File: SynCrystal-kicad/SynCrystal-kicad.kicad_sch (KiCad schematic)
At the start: 75 parts, among them J1 ICSP, J2 Projector, Q1 BC847, Q2 BC847, SW1 Mode -, SW2 Mode +, SW3 Frame -, SW4 Frame +, U1 74HCT14, U2 AP2210N-3.3TRG1, U3 AP63205WU, U4 LMC6482, U5 MCP4725, U6 TS5A3160, U7 ATmega328P, U8 ECS-TXO-3225MV-160-TR

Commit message: ERC progress
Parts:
- removed JP2: GND Ctrl, Jumper:SolderJumper-3_P1.3mm_Bridged12_RoundedPad1.0x1.5mm, symbol Jumper:SolderJumper_3_Bridged12
- removed R14, R15: 2k2, Resistor_SMD:R_0805_2012Metric, symbol Device:R
- removed U6: TS5A3160, Package_SON:Fairchild_MicroPak-6_1.0x1.45mm_P0.5mm, symbol Analog_Switch:FSA3157L6X
- added C15: 100n, Capacitor_SMD:C_0805_2012Metric, symbol Device:C_Small
- added JP3: VCC Ctrl, symbol Jumper:SolderJumper_3_Bridged12
- added TP8: Rx, Peacemans_Footprints:TestPoint_THTPad_1.5x1.5mm_Drill0.7mm_named, symbol Peacemans Teile:TestPoint_named
- added TP9: Tx, Peacemans_Footprints:TestPoint_THTPad_1.5x1.5mm_Drill0.7mm_named, symbol Peacemans Teile:TestPoint_named
- added unit 6 of U1
- added U6: TS5A3160DBV, Package_TO_SOT_SMD:SOT-23-6, symbol Analog_Switch:TS5A3160DBV
- JP1: value VCC Ctrl -> GND Ctrl; footprint Jumper:SolderJumper-3_P1.3mm_Bridged12_RoundedPad1.0x1.5mm -> (none); now left out of the parts list
- U5: symbol Analog_DAC:MCP4725 -> Analog_DAC:MCP4725xxx-xCH
- renumbered R16 to R14, R17 to R15, R18 to R16, R19 to R17, R20 to R18, R21 to R19, R22 to R20, R23 to R21, R24 to R22, TP8 to TP10, TP9 to TP11, TP10 to TP12
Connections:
- net 5V is gone; now on net +5V: C8.1, D3.1 (K), R8.2, U4.8 (V+)
- net +5V: now also U1.14 (VCC), C15.2, JP3.2 (C), U6.5 (V+); no longer JP1.2 (C)
- net GNDD: now also JP1.2 (C), U1.7 (GND), C15.1, JP3.3 (B), U6.2 (GND); no longer JP1.3 (B)
- net Pin 6-7-8: now also U6.4
- net RX: now also TP8.1
- net TX: now also TP9.1
- net at C13.2, R17.1: now also U1.13; no longer U1.11
- net at JP1.1 (A): now also D4.1 (GND); no longer D4.2 (VCC)
- net at R9.2: now also U6.1
- net +3V3 renamed +3.3V
- net A0 renamed P_POT
- net A1 renamed I_POT
- net A2 renamed D_POT
- net A3: no longer names the net of U7.26 (PC3)
- net D10 renamed Mode-
- net D11 renamed MOSI
- net D12 renamed Frame-
- net D13 renamed Frame+
- net D2 renamed INT0
- net D3 renamed INT1
- net D4: no longer names the net of U7.2 (PD4)
- net D5: no longer names the net of R22.1, U7.9 (PD5)
- net D6: no longer names the net of U7.10 (PD6)
- net D7: no longer names the net of TP11.1, U7.11 (PD7)
- net D9 renamed DAC_EN
- net DAC_EN: now also U6.6
- new net: D4.2 (VCC), JP1.3 (B), JP3.1 (A)
- new net: U1.11, U1.12
- no-connect marks 4 -> 7
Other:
- note added: "A0"
- note added: "A1"
- note added: "A2"
- note added: "A3"
- note added: "D10"
- note added: "D11"
- note added: "D12"
- note added: "D13"
- note added: "D2"
- note added: "D3"
- note added: "D4"
- note added: "D5"
- note added: "D6"
- note added: "D7"
- note added: "D8"
- note added: "D9"
- moved on the sheet: C11, C12, C13, C14, D3, D5, D6, Q2, R14, R15, R16, R17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

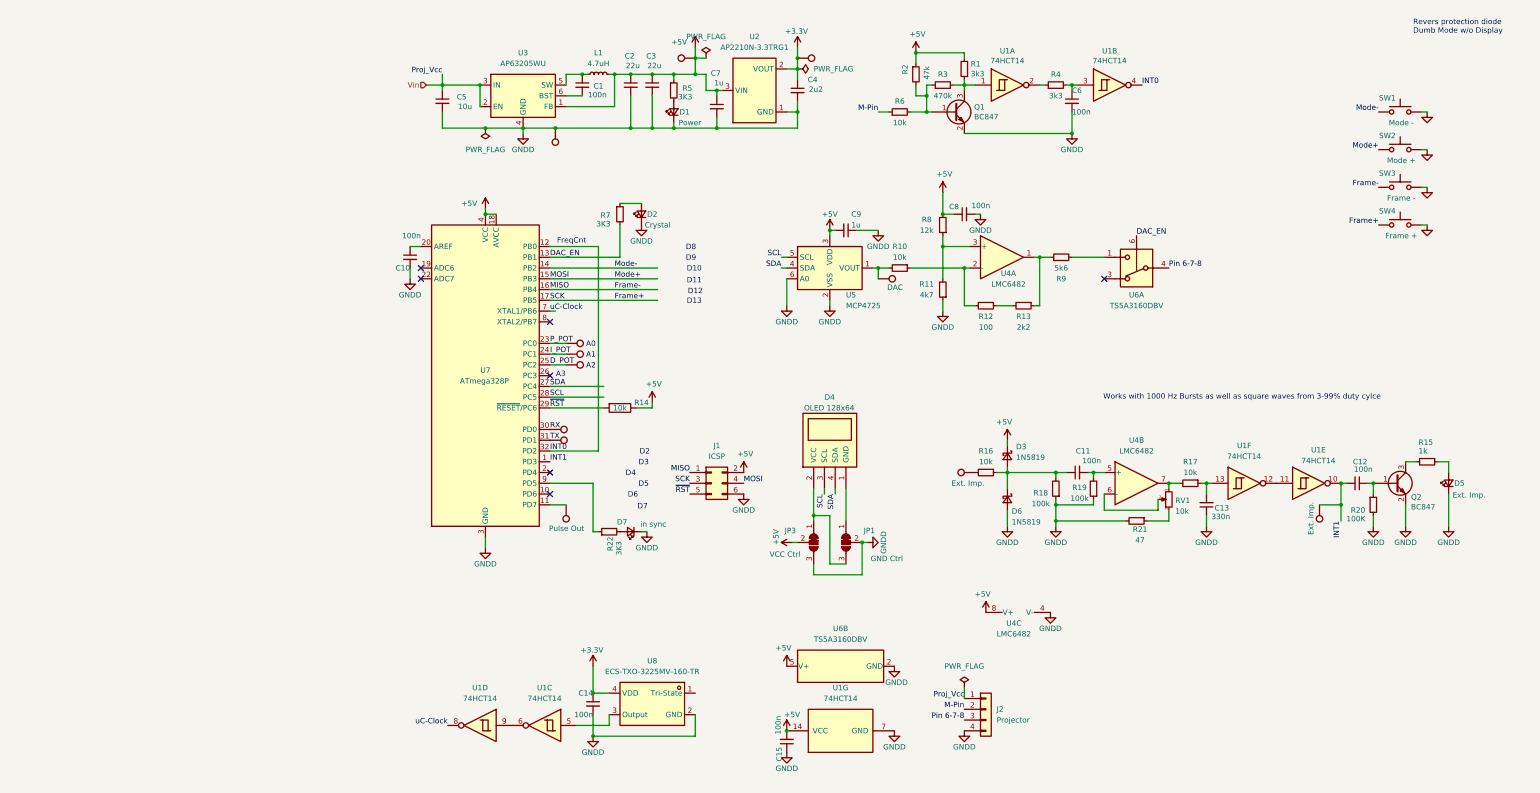
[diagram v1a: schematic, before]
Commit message: ERC clean, some pin changes for final PCB
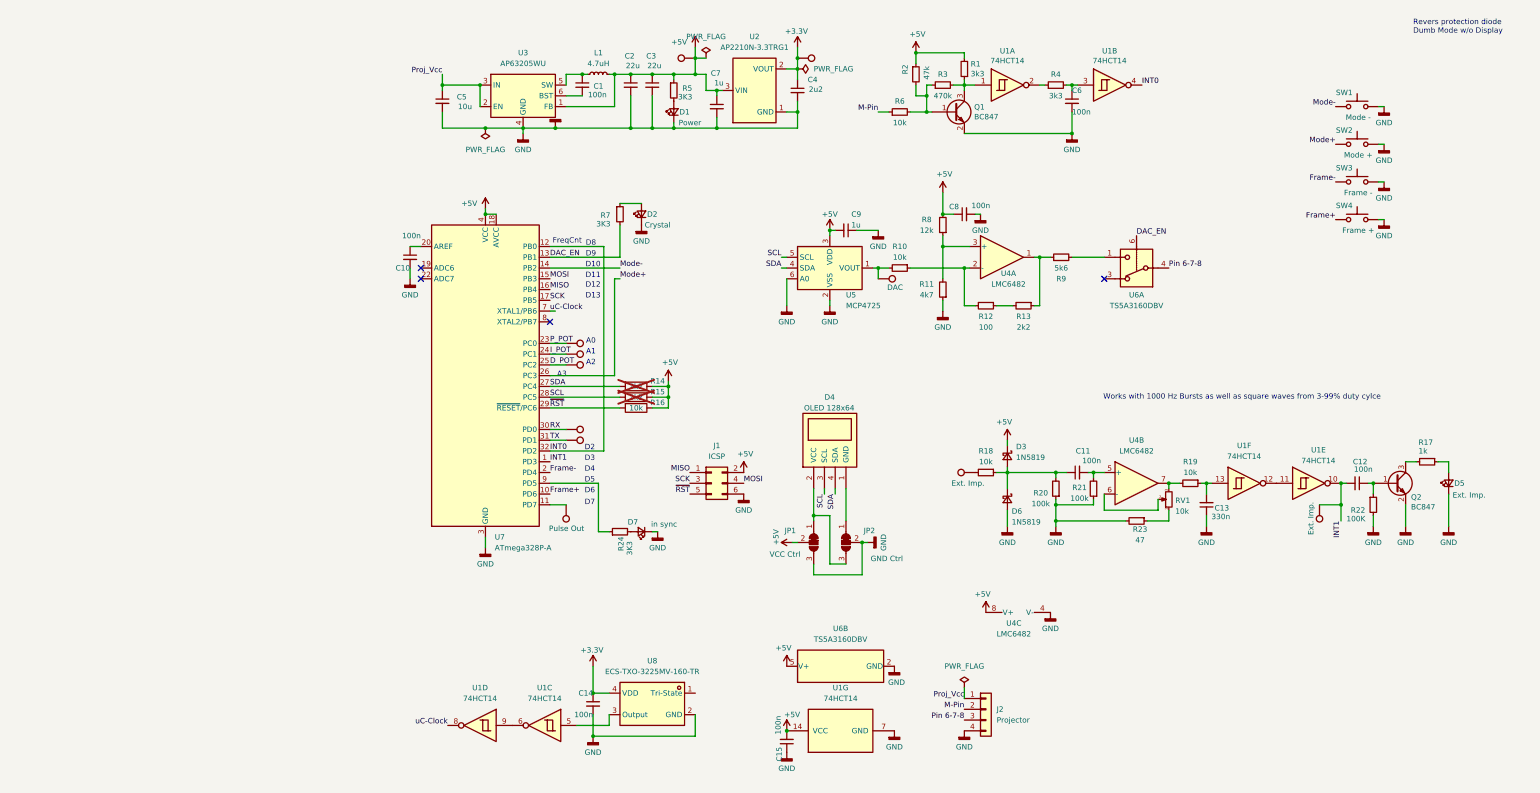
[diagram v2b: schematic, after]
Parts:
- removed TP3: GND, Peacemans_Footprints:TestPoint_THTPad_1.5x1.5mm_Drill0.7mm_named, symbol Peacemans Teile:TestPoint_named
- removed U7: ATmega328P, Package_QFP:TQFP-32_7x7mm_P0.8mm, symbol MCU_Microchip_ATmega:ATmega328P-AU
- added R14, R15: 2k2, Resistor_SMD:R_0805_2012Metric, symbol Device:R
- added U7: ATmega328P-A, Package_QFP:TQFP-32_7x7mm_P0.8mm, symbol MCU_Microchip_ATmega:ATmega328P-A
- renumbered JP3 to JP1, JP1 to JP2, R14 to R16, R15 to R17, R16 to R18, R17 to R19, R18 to R20, R19 to R21, R20 to R22, R21 to R23, R22 to R24, TP11 to TP10, TP12 to TP11, TP4 to TP3, TP5 to TP4, TP6 to TP5, TP7 to TP6, TP8 to TP7, TP9 to TP8, TP10 to TP9
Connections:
- net +5V: now also R14.1, R15.1, U7.18 (AVCC), U7.4 (VCC), U7.6 (VCC)
- net DAC_EN: now also U7.13 (PB1)
- net D_POT: now also U7.25 (PC2)
- net Frame+: now also U7.10 (PD6); no longer J1.3 (Pin_3)
- net Frame-: now also U7.2 (PD4); no longer J1.1 (Pin_1)
- net INT0: now also U7.12 (PB0), U7.32 (PD2)
- net INT1: now also U7.1 (PD3)
- net I_POT: now also U7.24 (PC1)
- net MOSI: now also U7.15 (PB3); no longer SW2.2
- net Mode-: now also U7.14 (PB2)
- net P_POT: now also U7.23 (PC0)
- net RX: now also U7.30 (PD0)
- net SCL: now also R15.2, U7.28 (PC5)
- net SDA: now also R14.2, U7.27 (PC4)
- net TX: now also U7.31 (PD1)
- net uC-Clock: now also U7.7 (XTAL1/PB6)
- net ~{RST}: now also U7.29 (~{RESET}/PC6)
- net at C10.1: now also U7.20 (AREF)
- net at TP10.1: now also U7.11 (PD7)
- net at R24.1: now also U7.9 (PD5)
- net GNDD renamed GND
- net GND: now also U7.21 (GND), U7.3 (GND), U7.5 (GND)
- net Vin renamed Proj_Vcc
- new net MISO: J1.1 (Pin_1), U7.16 (PB4)
- new net Mode+: SW2.2, U7.26 (PC3)
- new net SCK: J1.3 (Pin_3), U7.17 (PB5)
- no-connect marks 7 -> 4
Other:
- moved on the sheet: D7, R16, R24, SW1, SW2, SW3, SW4

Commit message: Most footprints
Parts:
- added D8: SL14D, Diode_SMD:D_SMA, symbol Device:D_Schottky_Small
- D3, D6: value 1N5819 -> SL14D; footprint (none) -> Diode_SMD:D_SMA
- D4: footprint Connector_PinHeader_2.54mm:PinHeader_1x04_P2.54mm_Horizontal_shorter -> Connector_PinHeader_2.54mm:PinHeader_1x04_P2.54mm_Vertical
- J1, SW1, SW2, SW3, SW4: footprint (none) -> Button_Switch_SMD:SW_Push_1P1T_NO_6x6mm_H9.5mm
- J2: footprint (none) -> Connector_PinHeader_2.54mm:PinHeader_1x04_P2.54mm_Horizontal
- JP1, JP2: footprint (none) -> Jumper:SolderJumper-3_P1.3mm_Bridged2Bar12_RoundedPad1.0x1.5mm
- L1: footprint (none) -> easyEDA:IND-SMD_L5.8-W5.2
- Q1, Q2: value BC847 -> SS8050
- R1, R10, R11, R12, R13, R14, R15, R16, R17, R18, R19, R2, R20, R21, R22, R23, R24, R3, R4, R5, R6, R7, R8, R9: footprint Resistor_SMD:R_0805_2012Metric -> Resistor_SMD:R_0603_1608Metric
- RV1: footprint (none) -> easyEDA:RES-TH_RK09K1110A0J_short
- TP1, TP10, TP2, TP3, TP4, TP5, TP6, TP7, TP8: footprint Peacemans_Footprints:TestPoint_THTPad_1.5x1.5mm_Drill0.7mm_named -> Peacemans Teile:TestPoint_THTPad_1.5x1.5mm_Drill0.7mm_named
- TP11: value Ext. Imp. -> Imp cln; footprint Peacemans_Footprints:TestPoint_THTPad_1.5x1.5mm_Drill0.7mm_named -> Peacemans Teile:TestPoint_THTPad_1.5x1.5mm_Drill0.7mm_named
- TP9: value Ext. Imp. -> Imp IN; footprint Peacemans_Footprints:TestPoint_THTPad_1.5x1.5mm_Drill0.7mm_named -> Peacemans Teile:TestPoint_THTPad_1.5x1.5mm_Drill0.7mm_named
- U1: footprint (none) -> Package_SO:SOIC-14_3.9x8.7mm_P1.27mm
- U2: footprint easyeda2kicad:SOT-23-3_L2.9-W1.3-P1.90-LS2.4-BR -> Package_TO_SOT_SMD:SOT-23-3
- U4: footprint (none) -> Peacemans Teile:TestPoint_THTPad_1.5x1.5mm_Drill0.7mm_named
- U8: footprint easyeda2kicad:OSC-SMD_4P-L3.2-W2.5-BL -> Crystal:Crystal_SMD_3225-4Pin_3.2x2.5mm
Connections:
- net Proj_Vcc: now also D8.2 (A); no longer C5.1, U3.2 (EN), U3.3 (IN)
- new net: C5.1, D8.1 (K), U3.2 (EN), U3.3 (IN)
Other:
- note added: "Dumb Mode w/o Display IR send"
- note removed: "Revers protection diode Dumb Mode w/o Display"

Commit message: PCB in progress
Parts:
- C1, C10, C11, C12, C13, C14, C15, C2, C3, C4, C5, C6, C7, C8, C9: footprint Capacitor_SMD:C_0805_2012Metric -> Capacitor_SMD:C_0603_1608Metric
- J1: footprint Button_Switch_SMD:SW_Push_1P1T_NO_6x6mm_H9.5mm -> Connector_PinHeader_2.54mm:PinHeader_2x03_P2.54mm_Vertical_displaced+
- L1: footprint easyEDA:IND-SMD_L5.8-W5.2 -> easyEDA:IND-SMD_L3.0-W3.0; LCSC (none) -> C527613; LCSC Part (none) -> C2929429
- R14, R15: now fitted
- TP1, TP10, TP11, TP2, TP3, TP4, TP5, TP6, TP7, TP8, TP9: footprint Peacemans Teile:TestPoint_THTPad_1.5x1.5mm_Drill0.7mm_named -> TestPoint:TestPoint_Pad_D1.0mm
- U1: footprint Package_SO:SOIC-14_3.9x8.7mm_P1.27mm -> Package_SO:TSSOP-14_4.4x5mm_P0.65mm; LCSC (none) -> C5968
- U4: footprint Peacemans Teile:TestPoint_THTPad_1.5x1.5mm_Drill0.7mm_named -> Package_SO:SOIC-8_3.9x4.9mm_P1.27mm
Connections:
- net +5V: now also R14.2; no longer R14.1
- net INT0: now also U1.10; no longer U1.4
- net INT1: now also U1.8; no longer U1.10
- net SDA: now also R14.1; no longer R14.2
- net uC-Clock: now also U1.6; no longer U1.8
- net at U1.5: now also U1.4; no longer U8.3 (Output)
- net at U1.9: now also U1.2; no longer U1.6
- net at Q1.3 (C), R1.1, R3.2: now also U1.13; no longer U1.1
- net at C13.2, R19.1: now also U1.1; no longer U1.13
- net at U1.11: now also C6.1, R4.2; no longer U1.12
- net at R4.1: now also U1.12; no longer U1.2
- new net: U1.3, U8.3 (Output)
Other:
- moved on the sheet: U1A, U1B, U1C, U1D, U1E, U1F

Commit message: More Footprint work
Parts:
- added CN1: PJ-342, easyEDA:AUDIO-SMD_PJ-342, symbol easyEDA:PJ-342
- added J3: ~, easyEDA:HDR-SMD_HX-PM2.54-1X4P-TP-YQ, symbol Connector:Conn_01x04_Socket
- added J4: ~, easyEDA:HDR-SMD_HX-PM2.54-1X4P-TP-YQ, symbol Connector:Conn_01x04_Pin
- D3: renamed from D4; footprint Connector_PinHeader_2.54mm:PinHeader_1x04_P2.54mm_Vertical -> Peacemans Teile:OLED_128x63_i2c_0.96
- J2: footprint Connector_PinHeader_2.54mm:PinHeader_1x04_P2.54mm_Horizontal -> easyEDA:CONN-TH_S4B-PH-KL-LF-SN
- RV1: footprint easyEDA:RES-TH_RK09K1110A0J_short -> easyEDA:RES-SMD_RK10J11R0A0H
- SW1, SW2, SW3, SW4: footprint Button_Switch_SMD:SW_Push_1P1T_NO_6x6mm_H9.5mm -> Button_Switch_SMD:SW_SPST_PTS647_Sx50
- renumbered C10 to C1, C9 to C10, C8 to C11, C6 to C12, C11 to C13, C13 to C14, C12 to C15, C5 to C2, C1 to C3, C14 to C4, C2 to C5, C3 to C6, C15 to C8, C4 to C9, D8 to D1, D1 to D2, D3 to D4, D6 to D5, D7 to D6, D2 to D7, D5 to D8, R14 to R1, R11 to R10, R1 to R11, R18 to R13, R13 to R14, R4 to R15, R20 to R16, R9 to R17, R21 to R18, R23 to R19, R15 to R2, R19 to R20, R24 to R21, R7 to R22, R17 to R23, R22 to R24, R16 to R3, R5 to R4, R6 to R5, R10 to R6, R2 to R7, R3 to R8, R8 to R9, TP4 to TP1, TP9 to TP10, TP5 to TP2, TP6 to TP3, TP7 to TP4, TP8 to TP5, TP10 to TP6, TP1 to TP7, TP2 to TP8, TP3 to TP9, U7 to U2, U8 to U4, U2 to U5, U5 to U6, U6 to U7, U4 to U8
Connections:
- net GND: now also J3.4 (Pin_4); no longer D6.1 (K), D7.1 (K), D8.1 (K)
- net at R21.1: now also J4.1 (Pin_1); no longer U2.9 (PD5)
- net at R22.1: now also J4.2 (Pin_2); no longer D7.2 (A)
- net at R23.2: now also J4.3 (Pin_3); no longer Q2.3 (C)
- net DAC_EN renamed Crystal_LED
- net Crystal_LED: now also J3.2 (Pin_2); no longer R22.2
- new net: D6.1 (K), D7.1 (K), D8.1 (K), J4.4 (Pin_4)
- new net: D7.2 (A), R22.2
- new net Ext_Imp_LED: J3.3 (Pin_3), Q2.3 (C)
- new net In_Sync-LED: J3.1 (Pin_1), U2.9 (PD5)
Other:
- moved on the sheet: D6, D7, D8, R21, R22, R23, SW1, SW2, SW3, SW4

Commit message: More schematics
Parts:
- removed C10, C7: 1u, Capacitor_SMD:C_0603_1608Metric, symbol Device:C_Small
- removed C11, C12, C13, C15, C3, C4: 100n, Capacitor_SMD:C_0603_1608Metric, symbol Device:C_Small
- removed C14: 330n, Capacitor_SMD:C_0603_1608Metric, symbol Device:C_Small
- removed C2: 10u, Capacitor_SMD:C_0603_1608Metric, symbol Device:C_Small
- removed C5, C6: 22u, Capacitor_SMD:C_0603_1608Metric, symbol Device:C_Small
- removed C9: 2u2, Capacitor_SMD:C_0603_1608Metric, symbol Device:C_Small
- removed D1, D4, D5: SL14D, Diode_SMD:D_SMA, symbol Device:D_Schottky_Small
- removed D2: Power, LED_SMD:LED_0805_2012Metric, symbol Device:LED_Small
- removed D3: OLED 128x64, Peacemans Teile:OLED_128x63_i2c_0.96, symbol Peacemans Teile:OLED-128-64-I2C-Display_Character
- removed D6: in sync, LED_SMD:LED_0805_2012Metric, symbol Device:LED_Small
- removed D7: Crystal, LED_SMD:LED_0805_2012Metric, symbol Device:LED_Small
- removed D8: Ext. Imp., LED_SMD:LED_0805_2012Metric, symbol Device:LED_Small
- removed J2: Projector, easyEDA:CONN-TH_S4B-PH-KL-LF-SN, symbol Connector_Generic:Conn_01x04
- removed J4: ~, easyEDA:HDR-SMD_HX-PM2.54-1X4P-TP-YQ, symbol Connector:Conn_01x04_Pin
- removed JP1: VCC Ctrl, Jumper:SolderJumper-3_P1.3mm_Bridged2Bar12_RoundedPad1.0x1.5mm, symbol Jumper:SolderJumper_3_Bridged12
- removed JP2: GND Ctrl, Jumper:SolderJumper-3_P1.3mm_Bridged2Bar12_RoundedPad1.0x1.5mm, symbol Jumper:SolderJumper_3_Bridged12
- removed L1: 4.7uH, easyEDA:IND-SMD_L3.0-W3.0, symbol Device:L_Small
- removed Q1, Q2: SS8050, Package_TO_SOT_SMD:SOT-23, symbol Transistor_BJT:BC847
- removed R10: 4k7, Resistor_SMD:R_0603_1608Metric, symbol Device:R_Small
- removed R11, R15: 3k3, Resistor_SMD:R_0603_1608Metric, symbol Device:R_Small
- removed R12: 100, Resistor_SMD:R_0603_1608Metric, symbol Device:R_Small
- removed R13, R20, R5, R6: 10k, Resistor_SMD:R_0603_1608Metric, symbol Device:R_Small
- removed R14: 2k2, Resistor_SMD:R_0603_1608Metric, symbol Device:R_Small
- removed R16, R18: 100k, Resistor_SMD:R_0603_1608Metric, symbol Device:R_Small
- removed R17: 5k6, Resistor_SMD:R_0603_1608Metric, symbol Device:R_Small
- removed R19: 47, Resistor_SMD:R_0603_1608Metric, symbol Device:R_Small
- removed R21, R22, R4: 3K3, Resistor_SMD:R_0603_1608Metric, symbol Device:R_Small
- removed R23: 1k, Resistor_SMD:R_0603_1608Metric, symbol Device:R_Small
- removed R24: 100K, Resistor_SMD:R_0603_1608Metric, symbol Device:R_Small
- removed R7: 47k, Resistor_SMD:R_0603_1608Metric, symbol Device:R_Small
- removed R8: 470k, Resistor_SMD:R_0603_1608Metric, symbol Device:R_Small
- removed R9: 12k, Resistor_SMD:R_0603_1608Metric, symbol Device:R_Small
- removed RV1: 10k, easyEDA:RES-SMD_RK10J11R0A0H, symbol Device:R_Potentiometer_Small
- removed SW1: Mode -, Button_Switch_SMD:SW_SPST_PTS647_Sx50, symbol Switch:SW_Push
- removed SW2: Mode +, Button_Switch_SMD:SW_SPST_PTS647_Sx50, symbol Switch:SW_Push
- removed SW3: Frame -, Button_Switch_SMD:SW_SPST_PTS647_Sx50, symbol Switch:SW_Push
- removed SW4: Frame +, Button_Switch_SMD:SW_SPST_PTS647_Sx50, symbol Switch:SW_Push
- removed TP10: Imp IN, TestPoint:TestPoint_Pad_D1.0mm, symbol Peacemans Teile:TestPoint_named
- removed TP11: Imp cln, TestPoint:TestPoint_Pad_D1.0mm, symbol Peacemans Teile:TestPoint_named
- removed TP7: 5V, TestPoint:TestPoint_Pad_D1.0mm, symbol Peacemans Teile:TestPoint_named
- removed TP8: 3V3, TestPoint:TestPoint_Pad_D1.0mm, symbol Peacemans Teile:TestPoint_named
- removed TP9: DAC, TestPoint:TestPoint_Pad_D1.0mm, symbol Peacemans Teile:TestPoint_named
- removed unit 3 of U1
- removed unit 5 of U1
- removed unit 6 of U1
- removed unit 4 of U1
- removed unit 2 of U1
- removed unit 1 of U1
- removed U3: AP63205WU, Package_TO_SOT_SMD:TSOT-23-6, symbol Regulator_Switching:AP63205WU
- removed U4: ECS-TXO-3225MV-160-TR, Crystal:Crystal_SMD_3225-4Pin_3.2x2.5mm, symbol easyEDA:ECS-TXO-3225MV-160-TR
- removed U5: AP2210N-3.3TRG1, Package_TO_SOT_SMD:SOT-23-3, symbol easyEDA:AP2210N-3.3TRG1
- removed U6: MCP4725, Package_TO_SOT_SMD:SOT-23-6, symbol Analog_DAC:MCP4725xxx-xCH
- removed unit 1 of U7
- removed unit 1 of U8
- removed unit 2 of U8
- added J2: DIN-6 Male, symbol Connector_Generic:Conn_01x07
- added R25, R26: 100k, Resistor_SMD:R_0603_1608Metric, symbol Device:R_Small
- added SW5: Shaft_Pulses, symbol Switch:SW_SP3T
- added TP13: D, TestPoint:TestPoint_Pad_D1.0mm, symbol Peacemans Teile:TestPoint_named
- TP6: value Pulse Out -> fps pulse
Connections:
- net +5V: now also R25.2, SW5.1
- net GND: now also J2.7 (Pin_7), R26.1, SW5.4
- net I_POT: now also U2.22 (ADC7); no longer U2.24 (PC1)
- net M-Pin: now also J2.2 (Pin_2)
- net MISO: now also TP6.1
- net MOSI: now also J2.6 (Pin_6)
- net P_POT: now also U2.19 (ADC6); no longer U2.23 (PC0)
- net Proj_Vcc: now also J2.1 (Pin_1)
- net Stop_EN: now reaches U2.11 (PD7)
- net Stop_EN: no longer TP6.1
- net Crystal_LED renamed DAC_EN
- net Ext_Imp_LED: no longer names the net of J3.3 (Pin_3)
- new net: SW5.3, U2.23 (PC0)
- new net: R25.1, R26.2, SW5.2
- new net Pin_678: J2.3 (Pin_3)
- new net Proj_starting: TP13.1, U2.24 (PC1)
- no-connect marks 4 -> 3
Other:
- added sheet DAC (DAC.kicad_sch)
- added sheet ESS in (ESS_in.kicad_sch)
- added sheet Frontpanel UI (Frontpanel.kicad_sch)
- added sheet PSU (PSU.kicad_sch)
- added sheet Projector Impulse Cleaning (Proj_Imp_Cleanup.kicad_sch)
- added sheet Projector_PCB (Projector_PCB.kicad_sch)
- added sheet TCXO (tcxo.kicad_sch)
- note added: "?"
- note added: "Use DIN-6 Connector (3 pluggable, 3 solderable, GND)"
- note added: "wozu Proj_starting pin? INT1 wegsparen? (2 Schottkys)"
- note removed: "Works with 1000 Hz Bursts as well as square waves from 3-99% duty cylce"
- moved on the sheet: C1, C8, CN1, J1, J3, R1, R2, R3, U1G, U2, U7B, U8C

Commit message: Projector PCB!
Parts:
- removed C8: 100n, Capacitor_SMD:C_0603_1608Metric, symbol Device:C_Small
- removed U1: 74HCT14, Package_SO:TSSOP-14_4.4x5mm_P0.65mm, symbol Peacemans Teile:74HCT14
- removed U7: TS5A3160DBV, Package_TO_SOT_SMD:SOT-23-6, symbol Analog_Switch:TS5A3160DBV
- removed U8: LMC6482, Package_SO:SOIC-8_3.9x4.9mm_P1.27mm, symbol Amplifier_Operational:LMC6482
- added R12: 100k, Resistor_SMD:R_0603_1608Metric, symbol Device:R
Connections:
- net +5V: now also R12.1
- net DAC_EN: now also J2.5 (Pin_5)
- net ESS in/Impulse_IN: now also CN1.5
- net GND: now also CN1.2, CN1.3, CN1.6, CN1.7
- net MOSI: no longer J2.6 (Pin_6)
- net Stop_EN: now also J2.4 (Pin_4), R12.2
- net Ext_Imp_LED: now reaches J3.3 (Pin_3)
- no-connect marks 3 -> 2
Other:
- removed sheet Projector_PCB
- sheet ESS in ports: added INT1; removed none
- note added: "Other imagineable pulse sources: - S/PDIF / TOSLINK Clock - Video FBAS - Pulse Head"
- note added: "Pulling this to GND (22k) indicates a connected lamp relais"
- note added: "To DIN-6 Plug (3 pluggable, 3 solderable + GND)"
- note added: "To Do: - Lampenrelais-Platine separieren - Frontpanel separieren - IR Receive - IR Out - Guide/Follow Selector - INT1 wegsparen? (2 Schottkys) - Startpiepser statt ESS Impulen erkennen"
- note removed: "?"
- note removed: "Dumb Mode w/o Display IR send"
- note removed: "Use DIN-6 Connector (3 pluggable, 3 solderable, GND)"
- note removed: "wozu Proj_starting pin? INT1 wegsparen? (2 Schottkys)"
- moved on the sheet: C1, CN1, J1, J2, J3, R1, R2, R25, R26, R3, SW5, U2
